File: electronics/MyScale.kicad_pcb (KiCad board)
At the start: 4 copper layers, 80 x 60 mm, 106 parts, among them J1 Conn_01x03, J10 Conn_02x03_Odd_Even, J11 Conn_01x02_MountingPin, J12 Conn_01x02_MountingPin, J2 Conn_01x03, J3 Conn_01x03, J4 Conn_01x03, J5 Conn_01x02_MountingPin, J7 SIM_Card, J8 Conn_01x02_MountingPin, J9 Conn_Coaxial_Small, Q1 SI2302CDS, Q2 SI2302CDS, Q4 PNP, SW1 SW_Push, SW3 SW_SPDT, U1 HX711, U2 TPS22953, U3 TXU0202, U5 STM32U083CCUx, U6 TPS7A0518PDBV, U7 TPS7A0533PDBV, U8 BQ25302RTER, Y1 Crystal

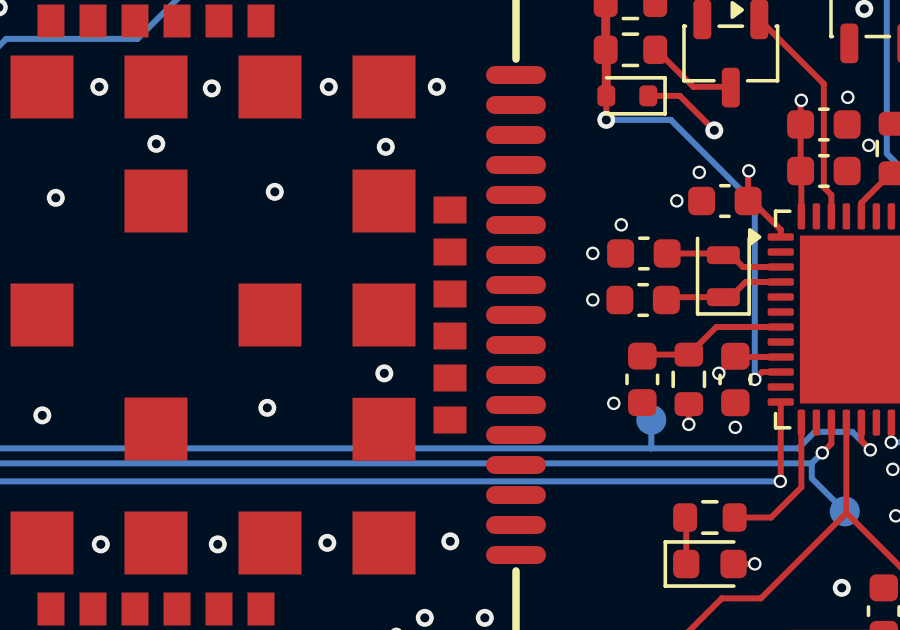
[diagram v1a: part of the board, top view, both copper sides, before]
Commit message: electronics: improve stencil openings for STM32
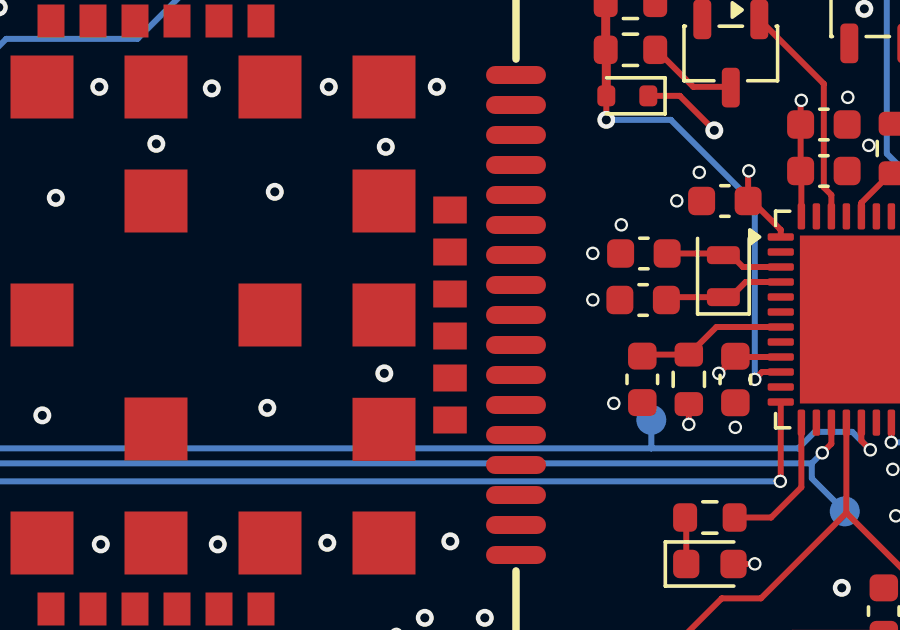
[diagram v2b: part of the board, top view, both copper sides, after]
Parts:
- U5: footprint Package_DFN_QFN:QFN-48-1EP_7x7mm_P0.5mm_EP5.6x5.6mm -> MyScale:QFN-48-1EP_7x7mm_P0.5mm_EP5.6x5.6mm
